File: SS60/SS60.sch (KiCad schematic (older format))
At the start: 4 parts

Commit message: 電気回路図-30
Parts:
- added J?: MYCONN3, symbol myLib:MYCONN3
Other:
- moved on the sheet: R?
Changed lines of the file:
@@
 L Device:R R?
 U 1 1 62124C17
-P 4280 5250
-F 0 "R?" V 4487 5250 50  0000 C CNN
-F 1 "100" V 4396 5250 50  0000 C CNN
-F 2 "" V 4210 5250 50  0001 C CNN
-F 3 "~" H 4280 5250 50  0001 C CNN
-	1    4280 5250
+P 4750 4900
+F 0 "R?" V 4957 4900 50  0000 C CNN
+F 1 "100" V 4866 4900 50  0000 C CNN
+F 2 "" V 4680 4900 50  0001 C CNN
+F 3 "~" H 4750 4900 50  0001 C CNN
+	1    4750 4900
 	0    -1   -1   0
 $EndComp
@@
 F 3 "http://ww1.microchip.com/downloads/en/devicedoc/40139e.pdf" H 3000 4650 50  0001 C CNN
 	1    3000 4650
-	1    0    0    -1
+	-1   0    0    -1
 $EndComp
 $Comp
@@
 	1    0    0    -1
 $EndComp
+$Comp
+L myLib:MYCONN3 J?
+U 1 1 62130A71
+P 4150 4650
+F 0 "J?" H 4050 4150 50  0000 C CNN
+F 1 "MYCONN3" H 4033 4634 50  0000 C CNN
+F 2 "" H 3950 4200 50  0001 C CNN
+F 3 "" H 3950 4200 50  0001 C CNN
+	1    4150 4650
+	1    0    0    -1
+$EndComp
+$Comp
+L power:VCC #PWR?
+U 1 1 6213273B
+P 4800 4000
+F 0 "#PWR?" H 4800 3850 50  0001 C CNN
+F 1 "VCC" H 4815 4173 50  0000 C CNN
+F 2 "" H 4800 4000 50  0001 C CNN
+F 3 "" H 4800 4000 50  0001 C CNN
+	1    4800 4000
+	1    0    0    -1
+$EndComp
+$Comp
+L power:VCC #PWR?
+U 1 1 6213391E
+P 3000 3550
+F 0 "#PWR?" H 3000 3400 50  0001 C CNN
+F 1 "VCC" H 3015 3723 50  0000 C CNN
+F 2 "" H 3000 3550 50  0001 C CNN
+F 3 "" H 3000 3550 50  0001 C CNN
+	1    3000 3550
+	1    0    0    -1
+$EndComp
+$Comp
+L power:VCC #PWR?
+U 1 1 62134AB5
+P 4450 4500
+F 0 "#PWR?" H 4450 4350 50  0001 C CNN
+F 1 "VCC" H 4465 4673 50  0000 C CNN
+F 2 "" H 4450 4500 50  0001 C CNN
+F 3 "" H 4450 4500 50  0001 C CNN
+	1    4450 4500
+	1    0    0    -1
+$EndComp
+$Comp
+L power:GND #PWR?
+U 1 1 62136123
+P 3000 5450
+F 0 "#PWR?" H 3000 5200 50  0001 C CNN
+F 1 "GND" H 3005 5277 50  0000 C CNN
+F 2 "" H 3000 5450 50  0001 C CNN
+F 3 "" H 3000 5450 50  0001 C CNN
+	1    3000 5450
+	1    0    0    -1
+$EndComp
+$Comp
+L power:GND #PWR?
+U 1 1 621366F3
+P 4400 5300
+F 0 "#PWR?" H 4400 5050 50  0001 C CNN
+F 1 "GND" H 4405 5127 50  0000 C CNN
+F 2 "" H 4400 5300 50  0001 C CNN
+F 3 "" H 4400 5300 50  0001 C CNN
+	1    4400 5300
+	1    0    0    -1
+$EndComp

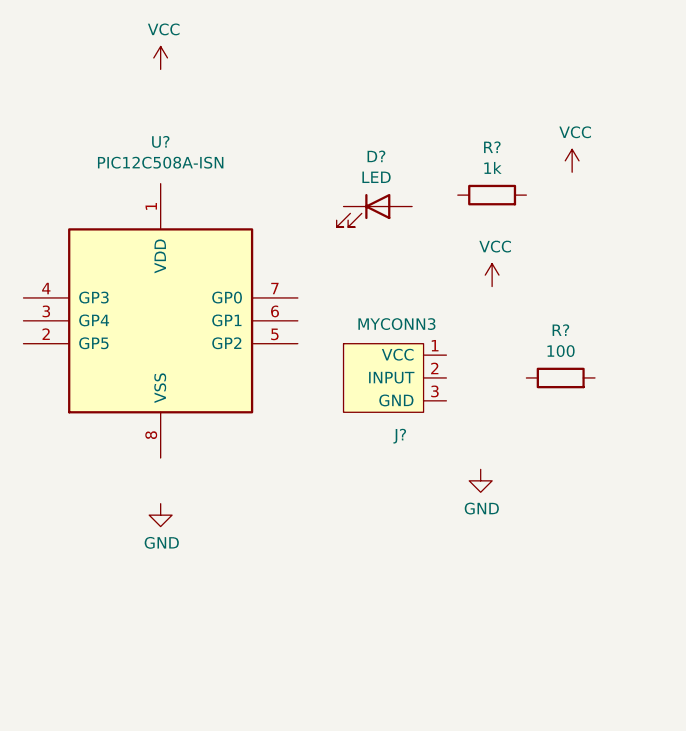
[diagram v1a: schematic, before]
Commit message: 54-Cvpcbで部品にフットプリントを割り付ける
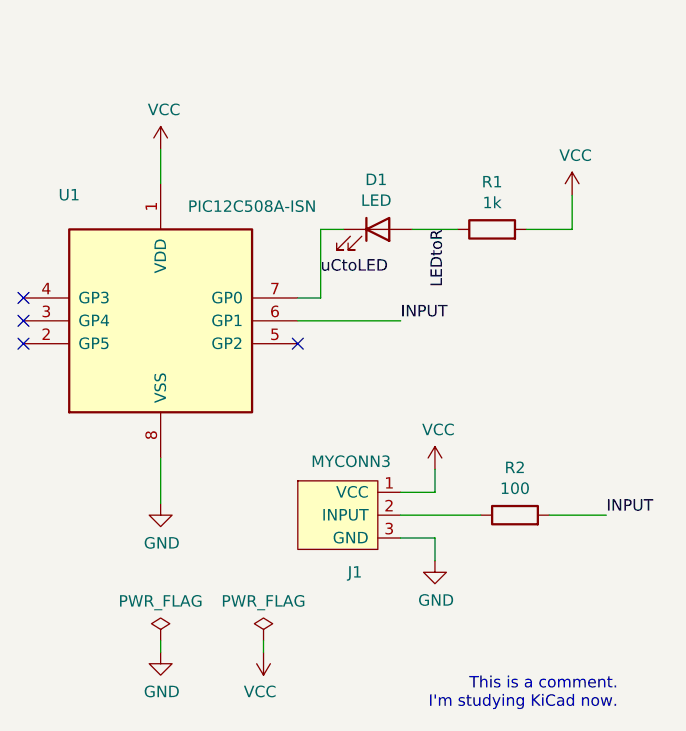
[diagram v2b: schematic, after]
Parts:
- D1: renamed from D?; footprint (none) -> LED_THT:LED_D5.0mm
- J1: renamed from J?; footprint (none) -> Connector:Banana_Jack_3Pin
- R1, R2: renamed from R?; footprint (none) -> Resistor_THT:R_Axial_DIN0207_L6.3mm_D2.5mm_P2.54mm_Vertical
- gave numbers to parts that had none: 1
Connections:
- net GND: now also J1.3 (GND), U1.8 (VSS)
- net VCC: now also J1.1 (VCC), R1.2, U1.1 (VDD)
- net LEDtoR: now reaches R1.1
- net LEDtoR: now also D1.2 (A)
- net at R2.1: now also J1.2 (INPUT)
- net INPUT: now reaches R2.2
- net INPUT: now also U1.6 (GP1)
- net uCtoLED: now reaches U1.7 (GP0)
- net uCtoLED: now also D1.1 (K)
- no-connect marks 0 -> 4
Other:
- note added: "This is a comment.\nI'm studying KiCad now."
- moved on the sheet: D1, J1, R1, R2
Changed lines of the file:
@@
 $EndDescr
 $Comp
-L Device:R R?
+L Device:R R1
 U 1 1 62123910
-P 4450 4100
-F 0 "R?" V 4657 4100 50  0000 C CNN
-F 1 "1k" V 4566 4100 50  0000 C CNN
-F 2 "" V 4380 4100 50  0001 C CNN
-F 3 "~" H 4450 4100 50  0001 C CNN
-	1    4450 4100
+P 4450 4250
+F 0 "R1" V 4657 4250 50  0000 C CNN
+F 1 "1k" V 4566 4250 50  0000 C CNN
+F 2 "Resistor_THT:R_Axial_DIN0207_L6.3mm_D2.5mm_P2.54mm_Vertical" V 4380 4250 50  0001 C CNN
+F 3 "~" H 4450 4250 50  0001 C CNN
+	1    4450 4250
 	0    -1   -1   0
 $EndComp
 $Comp
-L Device:R R?
+L Device:R R2
 U 1 1 62124C17
-P 4750 4900
-F 0 "R?" V 4957 4900 50  0000 C CNN
-F 1 "100" V 4866 4900 50  0000 C CNN
-F 2 "" V 4680 4900 50  0001 C CNN
-F 3 "~" H 4750 4900 50  0001 C CNN
-	1    4750 4900
+P 4550 5500
+F 0 "R2" V 4757 5500 50  0000 C CNN
+F 1 "100" V 4666 5500 50  0000 C CNN
+F 2 "Resistor_THT:R_Axial_DIN0207_L6.3mm_D2.5mm_P2.54mm_Vertical" V 4480 5500 50  0001 C CNN
+F 3 "~" H 4550 5500 50  0001 C CNN
+	1    4550 5500
 	0    -1   -1   0
 $EndComp
 $Comp
-L microchip_pic12mcu:PIC12C508A-ISN U?
+L microchip_pic12mcu:PIC12C508A-ISN U1
 U 1 1 62127763
 P 3000 4650
-F 0 "U?" H 3000 5431 50  0000 C CNN
-F 1 "PIC12C508A-ISN" H 3000 5340 50  0000 C CNN
+F 0 "U1" H 3400 5200 50  0000 C CNN
+F 1 "PIC12C508A-ISN" H 2600 5150 50  0000 C CNN
 F 2 "Package_DIP:DIP-8_W7.62mm" H 3600 5300 50  0001 C CNN
 F 3 "http://ww1.microchip.com/downloads/en/devicedoc/40139e.pdf" H 3000 4650 50  0001 C CNN
@@
 $EndComp
 $Comp
-L Device:LED D?
+L Device:LED D1
 U 1 1 6212CD06
-P 3950 4150
-F 0 "D?" H 3943 4367 50  0000 C CNN
-F 1 "LED" H 3943 4276 50  0000 C CNN
-F 2 "" H 3950 4150 50  0001 C CNN
-F 3 "~" H 3950 4150 50  0001 C CNN
-	1    3950 4150
-	1    0    0    -1
-$EndComp
-$Comp
-L myLib:MYCONN3 J?
+P 3950 4250
+F 0 "D1" H 3943 4467 50  0000 C CNN
+F 1 "LED" H 3943 4376 50  0000 C CNN
+F 2 "LED_THT:LED_D5.0mm" H 3950 4250 50  0001 C CNN
+F 3 "~" H 3950 4250 50  0001 C CNN
+	1    3950 4250
+	1    0    0    -1
+$EndComp
+$Comp
+L myLib:MYCONN3 J1
 U 1 1 62130A71
-P 4150 4650
-F 0 "J?" H 4050 4150 50  0000 C CNN
-F 1 "MYCONN3" H 4033 4634 50  0000 C CNN
-F 2 "" H 3950 4200 50  0001 C CNN
-F 3 "" H 3950 4200 50  0001 C CNN
-	1    4150 4650
-	1    0    0    -1
-$EndComp
-$Comp
-L power:VCC #PWR?
+P 3950 5250
+F 0 "J1" H 3850 4750 50  0000 C CNN
+F 1 "MYCONN3" H 3833 5234 50  0000 C CNN
+F 2 "Connector:Banana_Jack_3Pin" H 3750 4800 50  0001 C CNN
+F 3 "" H 3750 4800 50  0001 C CNN
+	1    3950 5250
+	1    0    0    -1
+$EndComp
+$Comp
+L power:VCC #PWR07
 U 1 1 6213273B
-P 4800 4000
-F 0 "#PWR?" H 4800 3850 50  0001 C CNN
-F 1 "VCC" H 4815 4173 50  0000 C CNN
-F 2 "" H 4800 4000 50  0001 C CNN
-F 3 "" H 4800 4000 50  0001 C CNN
-	1    4800 4000
-	1    0    0    -1
-$EndComp
-$Comp
-L power:VCC #PWR?
+P 4800 4100
+F 0 "#PWR07" H 4800 3950 50  0001 C CNN
+F 1 "VCC" H 4815 4273 50  0000 C CNN
+F 2 "" H 4800 4100 50  0001 C CNN
+F 3 "" H 4800 4100 50  0001 C CNN
+	1    4800 4100
+	1    0    0    -1
+$EndComp
+$Comp
+L power:VCC #PWR01
 U 1 1 6213391E
-P 3000 3550
-F 0 "#PWR?" H 3000 3400 50  0001 C CNN
-F 1 "VCC" H 3015 3723 50  0000 C CNN
-F 2 "" H 3000 3550 50  0001 C CNN
-F 3 "" H 3000 3550 50  0001 C CNN
-	1    3000 3550
-	1    0    0    -1
-$EndComp
-$Comp
-L power:VCC #PWR?
+P 3000 3900
+F 0 "#PWR01" H 3000 3750 50  0001 C CNN
+F 1 "VCC" H 3015 4073 50  0000 C CNN
+F 2 "" H 3000 3900 50  0001 C CNN
+F 3 "" H 3000 3900 50  0001 C CNN
+	1    3000 3900
+	1    0    0    -1
+$EndComp
+$Comp
+L power:VCC #PWR05
 U 1 1 62134AB5
-P 4450 4500
-F 0 "#PWR?" H 4450 4350 50  0001 C CNN
-F 1 "VCC" H 4465 4673 50  0000 C CNN
-F 2 "" H 4450 4500 50  0001 C CNN
-F 3 "" H 4450 4500 50  0001 C CNN
-	1    4450 4500
-	1    0    0    -1
-$EndComp
-$Comp
-L power:GND #PWR?
+P 4200 5300
+F 0 "#PWR05" H 4200 5150 50  0001 C CNN
+F 1 "VCC" H 4215 5473 50  0000 C CNN
+F 2 "" H 4200 5300 50  0001 C CNN
+F 3 "" H 4200 5300 50  0001 C CNN
+	1    4200 5300
+	1    0    0    -1
+$EndComp
+$Comp
+L power:GND #PWR02
 U 1 1 62136123
 P 3000 5450
-F 0 "#PWR?" H 3000 5200 50  0001 C CNN
+F 0 "#PWR02" H 3000 5200 50  0001 C CNN
 F 1 "GND" H 3005 5277 50  0000 C CNN
 F 2 "" H 3000 5450 50  0001 C CNN
@@
 $EndComp
 $Comp
-L power:GND #PWR?
+L power:GND #PWR06
 U 1 1 621366F3
-P 4400 5300
-F 0 "#PWR?" H 4400 5050 50  0001 C CNN
-F 1 "GND" H 4405 5127 50  0000 C CNN
-F 2 "" H 4400 5300 50  0001 C CNN
-F 3 "" H 4400 5300 50  0001 C CNN
-	1    4400 5300
-	1    0    0    -1
-$EndComp
+P 4200 5700
+F 0 "#PWR06" H 4200 5450 50  0001 C CNN
+F 1 "GND" H 4205 5527 50  0000 C CNN
+F 2 "" H 4200 5700 50  0001 C CNN
+F 3 "" H 4200 5700 50  0001 C CNN
+	1    4200 5700
+	1    0    0    -1
+$EndComp
+Wire Wire Line
+	4300 4250 4100 4250
+Wire Wire Line
+	4800 4100 4800 4250
+Wire Wire Line
+	4800 4250 4600 4250
+Wire Wire Line
+	3800 4250 3700 4250
+Wire Wire Line
+	3700 4250 3700 4550
+Wire Wire Line
+	3700 4550 3600 4550
+Wire Wire Line
+	3600 4650 4050 4650
+Wire Wire Line
+	3000 3900 3000 4050
+Wire Wire Line
+	3000 5250 3000 5450
+Wire Wire Line
+	4200 5300 4200 5400
+Wire Wire Line
+	4200 5400 4050 5400
+Wire Wire Line
+	4050 5500 4400 5500
+Wire Wire Line
+	4050 5600 4200 5600
+Wire Wire Line
+	4200 5600 4200 5700
+Wire Wire Line
+	4700 5500 4950 5500
+Text Label 4050 4650 0    50   ~ 0
+INPUT
+Text Label 4950 5500 0    50   ~ 0
+INPUT
+Text Label 3700 4450 0    50   ~ 0
+uCtoLED
+Text Label 4250 4250 3    50   ~ 0
+LEDtoR
+NoConn ~ 3600 4750
+NoConn ~ 2400 4750
+NoConn ~ 2400 4650
+NoConn ~ 2400 4550
+$Comp
+L power:PWR_FLAG #FLG01
+U 1 1 6213F08B
+P 3000 6050
+F 0 "#FLG01" H 3000 6125 50  0001 C CNN
+F 1 "PWR_FLAG" H 3000 6223 50  0000 C CNN
+F 2 "" H 3000 6050 50  0001 C CNN
+F 3 "~" H 3000 6050 50  0001 C CNN
+	1    3000 6050
+	1    0    0    -1
+$EndComp
+$Comp
+L power:PWR_FLAG #FLG02
+U 1 1 621401C9
+P 3450 6050
+F 0 "#FLG02" H 3450 6125 50  0001 C CNN
+F 1 "PWR_FLAG" H 3450 6223 50  0000 C CNN
+F 2 "" H 3450 6050 50  0001 C CNN
+F 3 "~" H 3450 6050 50  0001 C CNN
+	1    3450 6050
+	1    0    0    -1
+$EndComp
+$Comp
+L power:GND #PWR03
+U 1 1 62140CD9
+P 3000 6100
+F 0 "#PWR03" H 3000 5850 50  0001 C CNN
+F 1 "GND" H 3005 5927 50  0000 C CNN
+F 2 "" H 3000 6100 50  0001 C CNN
+F 3 "" H 3000 6100 50  0001 C CNN
+	1    3000 6100
+	1    0    0    -1
+$EndComp
+$Comp
+L power:VCC #PWR04
+U 1 1 62141B0D
+P 3450 6100
+F 0 "#PWR04" H 3450 5950 50  0001 C CNN
+F 1 "VCC" H 3465 6273 50  0000 C CNN
+F 2 "" H 3450 6100 50  0001 C CNN
+F 3 "" H 3450 6100 50  0001 C CNN
+	1    3450 6100
+	-1   0    0    1
+$EndComp
+Wire Wire Line
+	3000 6050 3000 6100
+Text Notes 5000 6350 2    50   ~ 0
+This is a comment.\nI'm studying KiCad now.
+Wire Wire Line
+	3450 6050 3450 6100
 $EndSCHEMATC
